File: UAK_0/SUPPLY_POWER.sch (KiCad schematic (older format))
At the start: 23 parts, among them X1 Крепежное_отверстие_d2, X2 Крепежное_отверстие_d2, X3 Крепежное_отверстие_d2

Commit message: BOOT&PRG, концевик, ЖК, звук, подсветка - без трассировки
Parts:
- R1: INFO 100кОм -> 100 кОм
- R2: INFO 6,8кОм -> 6,8 кОм
- R3: INFO 44,2кОм -> 44,2 кОм
- R4: INFO 10кОм -> 10 кОм
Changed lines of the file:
@@
 EESchema Schematic File Version 4
+LIBS:UAK_0-cache
 EELAYER 30 0
 EELAYER END
@@
 F 2 "N_RLC:Конденсатор_SMD_0603" H 5650 2750 60  0001 C CNN
 F 3 "" H 5650 2750 60  0001 C CNN
-F 4 "10нФ/100В" H 5650 2850 50  0000 C CNN "INFO"
+F 4 "10нФ/100В" H 5700 2850 50  0000 C CNN "INFO"
 F 5 "https://www.chipdip.ru/product/grm188r72a103ka01d" H 5650 2750 50  0001 C CNN "LINK"
 	1    5650 2750
@@
 F 2 "N_RLC:Резистор_SMD_0603_0,065_Вт" H 3200 2900 60  0001 C CNN
 F 3 "" H 3200 2900 60  0001 C CNN
-F 4 "100кОм" H 3200 2750 50  0000 C CNN "INFO"
+F 4 "100 кОм" H 3200 2750 50  0000 C CNN "INFO"
 F 5 "" H 3200 3048 50  0001 C CNN "LINK"
 	1    3200 2900
@@
 F 2 "N_RLC:Резистор_SMD_0603_0,065_Вт" H 3250 3550 60  0001 C CNN
 F 3 "" H 3250 3550 60  0001 C CNN
-F 4 "6,8кОм" V 3303 3653 50  0000 L CNN "INFO"
+F 4 "6,8 кОм" V 3303 3653 50  0000 L CNN "INFO"
 F 5 "" H 3250 3698 50  0001 C CNN "LINK"
 	1    3250 3550
@@
 F 2 "N_RLC:Резистор_SMD_0603_0,065_Вт" H 7000 4550 60  0001 C CNN
 F 3 "" H 7000 4550 60  0001 C CNN
-F 4 "10кОм" V 7050 4200 50  0000 L CNN "INFO"
+F 4 "10 кОм" V 7050 4150 50  0000 L CNN "INFO"
 F 5 "" H 7000 4698 50  0001 C CNN "LINK"
 	1    7000 4550
@@
 F 2 "N_RLC:Резистор_SMD_0603_0,065_Вт" H 7000 3550 60  0001 C CNN
 F 3 "" H 7000 3550 60  0001 C CNN
-F 4 "44,2кОм" V 7050 3150 50  0000 L CNN "INFO"
+F 4 "44,2 кОм" V 7050 3100 50  0000 L CNN "INFO"
 F 5 "" H 7000 3698 50  0001 C CNN "LINK"
 	1    7000 3550
@@
 	7000 3850 7000 4050
 Wire Wire Line
-	5000 3200 5500 3200
-Text Label 5500 3200 2    50   ~ 0
+	5000 3200 5250 3200
+Text Label 5250 3200 2    50   ~ 0
 GND
 Wire Wire Line
@@
 Wire Wire Line
 	3500 2900 3850 2900
-Text Label 5500 2900 2    50   ~ 0
+Text Label 5250 2900 2    50   ~ 0
 12V
 Wire Wire Line
-	5500 2900 5000 2900
+	5250 2900 5000 2900
 Text Label 2250 2900 0    50   ~ 0
 12V

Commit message: нет коммутации 220В, остальная схема есть, нет трассировка
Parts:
- added VD4, VD5: Диод_шоттки_SK16, N_VD_HL:Диод_SMB, symbol elements_2020:Диод_шоттки_SK16
- renumbered C4 to C10, C5 to C11, C7 to C12, C6 to C13, C9 to C14, C10 to C15, C8 to C16, C1 to C7, C2 to C8, C3 to C9, DD1 to DD2, R1 to R15, R2 to R16, R3 to R17, R4 to R18, X1 to X5, X2 to X6, X3 to X7
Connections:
- net at C13.1, L2.6: now also VD4.2, VD5.2; no longer G1.+V
- net 0V_RESERV: now reaches C13.2, G1.-V, L2.4
- new net: G1.+V, VD5.1
- new net 12V_RESERV: VD4.1
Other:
- moved on the sheet: C11, C12, C13, C14, C15, C16, C7, C8, C9, DD2, G2, L1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

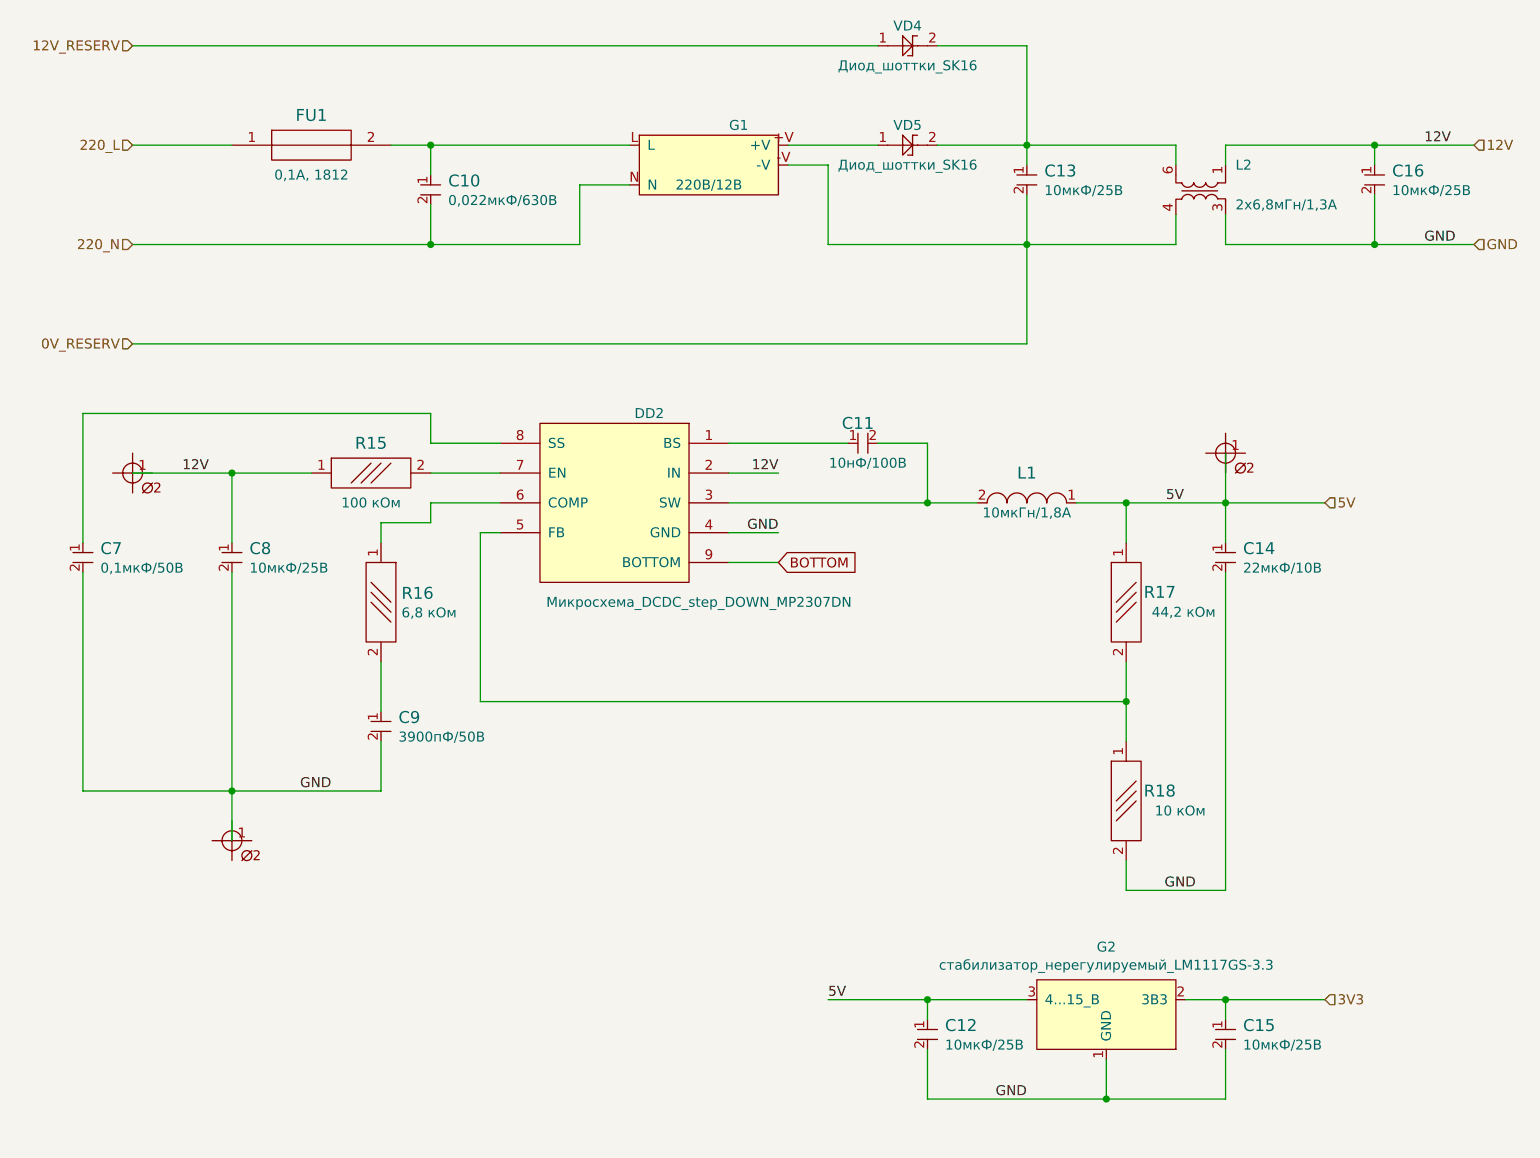
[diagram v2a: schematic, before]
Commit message: подготовлена схема, нет трассировки
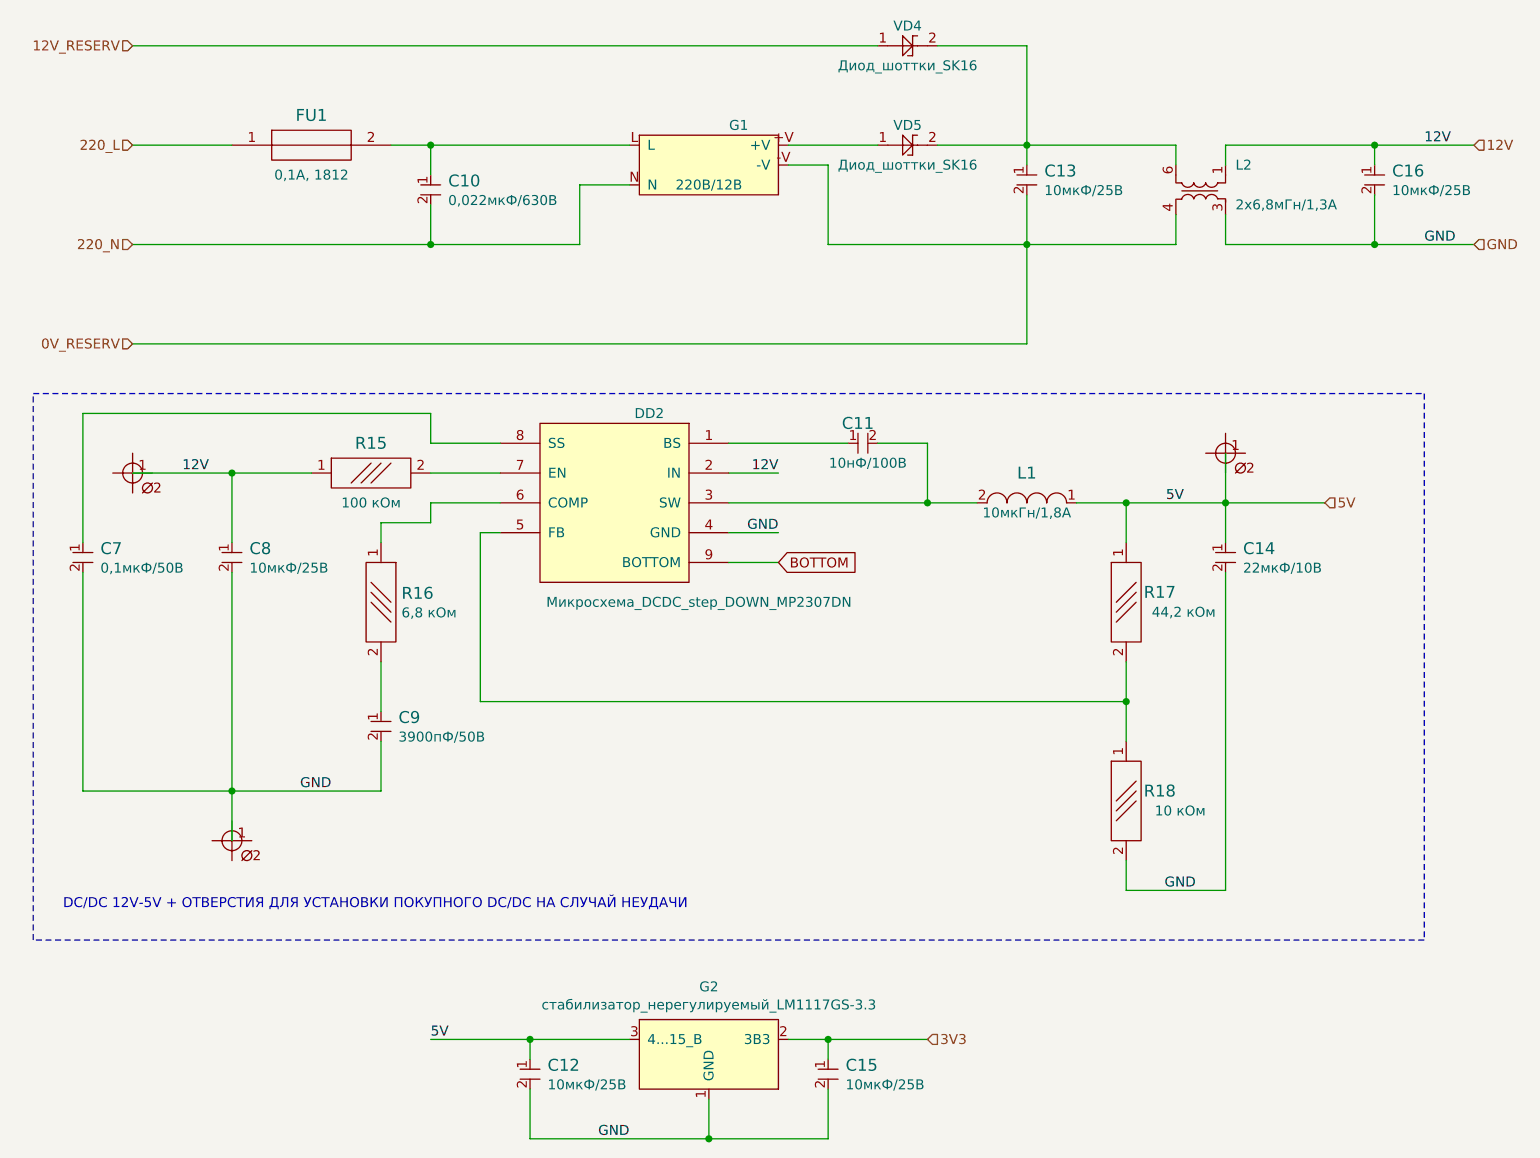
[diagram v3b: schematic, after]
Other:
- note added: "DC/DC 12V-5V + ОТВЕРСТИЯ ДЛЯ УСТАНОВКИ ПОКУПНОГО DC/DC НА СЛУЧАЙ НЕУДАЧИ"
- moved on the sheet: C12, C15, G2
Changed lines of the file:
@@
 Text HLabel 8750 2000 2    50   Input ~ 0
 GND
-Text HLabel 8000 5800 2    50   Input ~ 0
+Text HLabel 6000 6000 2    50   Input ~ 0
 3V3
 Text HLabel 8000 3300 2    50   Input ~ 0
@@
 L elements:стабилизатор_нерегулируемый_LM1117S33 G2
 U 1 1 5F5A8D81
-P 6550 5800
-F 0 "G2" H 6900 6065 50  0000 C CNN
-F 1 "стабилизатор_нерегулируемый_LM1117GS-3.3" H 6900 5974 50  0000 C CNN
-F 2 "N_VD_HL:Транзистор_NPN_SOT223" H 6550 5800 50  0001 C CNN
-F 3 "https://static.chipdip.ru/lib/138/DOC004138838.pdf" H 6550 5800 50  0001 C CNN
-F 4 "https://www.chipdip.ru/product/lm1117gs-3.3" H 6550 5800 50  0001 C CNN "LINK"
-	1    6550 5800
+P 4550 6000
+F 0 "G2" H 4900 6265 50  0000 C CNN
+F 1 "стабилизатор_нерегулируемый_LM1117GS-3.3" H 4900 6174 50  0000 C CNN
+F 2 "N_VD_HL:Транзистор_NPN_SOT223" H 4550 6000 50  0001 C CNN
+F 3 "https://static.chipdip.ru/lib/138/DOC004138838.pdf" H 4550 6000 50  0001 C CNN
+F 4 "https://www.chipdip.ru/product/lm1117gs-3.3" H 4550 6000 50  0001 C CNN "LINK"
+	1    4550 6000
 	1    0    0    -1
 $EndComp
@@
 L elements:Конденсатор_керамический C?
 U 1 1 5F5A914F
-P 6000 5950
+P 4000 6150
 AR Path="/5F5A914F" Ref="C?"  Part="1"
 AR Path="/5F540B17/5F5A914F" Ref="C12"  Part="1"
-F 0 "C12" V 5980 6038 60  0000 L CNN
-F 1 "Конденсатор_керамический" H 6100 5850 60  0001 C CNN
-F 2 "N_RLC:Конденсатор_SMD_0603" H 6000 5950 60  0001 C CNN
-F 3 "" H 6000 5950 60  0001 C CNN
-F 4 "10мкФ/25В" V 6078 6038 50  0000 L CNN "INFO"
-F 5 "https://www.chipdip.ru/product/grm188r61e106m" H 6000 5950 50  0001 C CNN "LINK"
-	1    6000 5950
+F 0 "C12" V 3980 6238 60  0000 L CNN
+F 1 "Конденсатор_керамический" H 4100 6050 60  0001 C CNN
+F 2 "N_RLC:Конденсатор_SMD_0603" H 4000 6150 60  0001 C CNN
+F 3 "" H 4000 6150 60  0001 C CNN
+F 4 "10мкФ/25В" V 4078 6238 50  0000 L CNN "INFO"
+F 5 "https://www.chipdip.ru/product/grm188r61e106m" H 4000 6150 50  0001 C CNN "LINK"
+	1    4000 6150
 	0    1    1    0
 $EndComp
@@
 L elements:Конденсатор_керамический C?
 U 1 1 5F5AA72C
-P 7500 5950
+P 5500 6150
 AR Path="/5F5AA72C" Ref="C?"  Part="1"
 AR Path="/5F540B17/5F5AA72C" Ref="C15"  Part="1"
-F 0 "C15" V 7480 6038 60  0000 L CNN
-F 1 "Конденсатор_керамический" H 7600 5850 60  0001 C CNN
-F 2 "N_RLC:Конденсатор_SMD_0603" H 7500 5950 60  0001 C CNN
-F 3 "" H 7500 5950 60  0001 C CNN
-F 4 "10мкФ/25В" V 7578 6038 50  0000 L CNN "INFO"
-F 5 "https://www.chipdip.ru/product/grm188r61e106m" H 7500 5950 50  0001 C CNN "LINK"
-	1    7500 5950
-	0    1    1    0
-$EndComp
-Wire Wire Line
-	7300 5800 7500 5800
-Wire Wire Line
-	7500 5800 7500 5900
-Wire Wire Line
-	7500 6050 7500 6300
-Wire Wire Line
-	7500 6300 6900 6300
-Wire Wire Line
-	6000 6300 6000 6050
-Wire Wire Line
-	6000 5900 6000 5800
-Wire Wire Line
-	6000 5800 6500 5800
-Connection ~ 6900 6300
-Wire Wire Line
-	6900 6300 6000 6300
-Wire Wire Line
-	6900 6100 6900 6300
-Text Label 6500 6300 2    50   ~ 0
+F 0 "C15" V 5480 6238 60  0000 L CNN
+F 1 "Конденсатор_керамический" H 5600 6050 60  0001 C CNN
+F 2 "N_RLC:Конденсатор_SMD_0603" H 5500 6150 60  0001 C CNN
+F 3 "" H 5500 6150 60  0001 C CNN
+F 4 "10мкФ/25В" V 5578 6238 50  0000 L CNN "INFO"
+F 5 "https://www.chipdip.ru/product/grm188r61e106m" H 5500 6150 50  0001 C CNN "LINK"
+	1    5500 6150
+	0    1    1    0
+$EndComp
+Wire Wire Line
+	5300 6000 5500 6000
+Wire Wire Line
+	5500 6000 5500 6100
+Wire Wire Line
+	5500 6250 5500 6500
+Wire Wire Line
+	5500 6500 4900 6500
+Wire Wire Line
+	4000 6500 4000 6250
+Wire Wire Line
+	4000 6100 4000 6000
+Wire Wire Line
+	4000 6000 4500 6000
+Connection ~ 4900 6500
+Wire Wire Line
+	4900 6500 4000 6500
+Wire Wire Line
+	4900 6300 4900 6500
+Text Label 4500 6500 2    50   ~ 0
 GND
 Wire Wire Line
-	6000 5800 5500 5800
-Connection ~ 6000 5800
-Wire Wire Line
-	7500 5800 8000 5800
-Connection ~ 7500 5800
+	4000 6000 3500 6000
+Connection ~ 4000 6000
+Wire Wire Line
+	5500 6000 6000 6000
+Connection ~ 5500 6000
 Text Label 7200 3300 0    50   ~ 0
 5V
-Text Label 5500 5800 0    50   ~ 0
+Text Label 3500 6000 0    50   ~ 0
 5V
 $Comp
@@
 Wire Wire Line
 	6500 2500 6500 2000
+Wire Notes Line
+	1500 2750 8500 2750
+Wire Notes Line
+	8500 2750 8500 5500
+Wire Notes Line
+	8500 5500 1500 5500
+Wire Notes Line
+	1500 5500 1500 2750
+Text Notes 1650 5350 0    50   ~ 0
+DC/DC 12V-5V + ОТВЕРСТИЯ ДЛЯ УСТАНОВКИ ПОКУПНОГО DC/DC НА СЛУЧАЙ НЕУДАЧИ
 $EndSCHEMATC

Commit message: есть трассировка питания
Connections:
- net 12V_OUT_G: now reaches G1.+V, VD5.1
- net 220_L_FU: now reaches C10.1, FU1.2, G1.L
- net 12V_NOISE: now reaches C13.1, L2.6, VD4.2, VD5.2
- net 5V_DC-DC: now reaches C11.2, DD2.3 (SW), L1.2
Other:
- moved on the sheet: VD4, VD5
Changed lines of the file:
@@
 L elements_2020:Диод_шоттки_SK16 VD?
 U 1 1 5F83EC0D
-P 5750 1000
+P 6000 1000
 AR Path="/5F83EC0D" Ref="VD?"  Part="1"
 AR Path="/5F540B17/5F83EC0D" Ref="VD4"  Part="1"
-F 0 "VD4" H 5900 1100 50  0000 C CNN
-F 1 "Диод_шоттки_SK16" H 5900 900 50  0000 C CNN
-F 2 "N_VD_HL:Диод_SMB" H 5925 775 50  0001 C CNN
-F 3 "https://static.chipdip.ru/lib/046/DOC003046730.pdf" H 5650 1000 50  0001 C CNN
-F 4 "1А, 60В" H 5925 550 50  0001 C CNN "INFO"
-F 5 "https://www.chipdip.ru/product/sk16-diotec" H 5925 675 50  0001 C CNN "LINK"
-	1    5750 1000
+F 0 "VD4" H 6150 1100 50  0000 C CNN
+F 1 "Диод_шоттки_SK16" H 6050 900 50  0000 C CNN
+F 2 "N_VD_HL:Диод_SMB" H 6175 775 50  0001 C CNN
+F 3 "https://static.chipdip.ru/lib/046/DOC003046730.pdf" H 5900 1000 50  0001 C CNN
+F 4 "1А, 60В" H 6175 550 50  0001 C CNN "INFO"
+F 5 "https://www.chipdip.ru/product/sk16-diotec" H 6175 675 50  0001 C CNN "LINK"
+	1    6000 1000
 	1    0    0    -1
 $EndComp
@@
 L elements_2020:Диод_шоттки_SK16 VD?
 U 1 1 5F8429E0
-P 5750 1500
+P 6000 1500
 AR Path="/5F8429E0" Ref="VD?"  Part="1"
 AR Path="/5F540B17/5F8429E0" Ref="VD5"  Part="1"
-F 0 "VD5" H 5900 1600 50  0000 C CNN
-F 1 "Диод_шоттки_SK16" H 5900 1400 50  0000 C CNN
-F 2 "N_VD_HL:Диод_SMB" H 5925 1275 50  0001 C CNN
-F 3 "https://static.chipdip.ru/lib/046/DOC003046730.pdf" H 5650 1500 50  0001 C CNN
-F 4 "1А, 60В" H 5925 1050 50  0001 C CNN "INFO"
-F 5 "https://www.chipdip.ru/product/sk16-diotec" H 5925 1175 50  0001 C CNN "LINK"
-	1    5750 1500
+F 0 "VD5" H 6150 1600 50  0000 C CNN
+F 1 "Диод_шоттки_SK16" H 6050 1400 50  0000 C CNN
+F 2 "N_VD_HL:Диод_SMB" H 6175 1275 50  0001 C CNN
+F 3 "https://static.chipdip.ru/lib/046/DOC003046730.pdf" H 5900 1500 50  0001 C CNN
+F 4 "1А, 60В" H 6175 1050 50  0001 C CNN "INFO"
+F 5 "https://www.chipdip.ru/product/sk16-diotec" H 6175 1175 50  0001 C CNN "LINK"
+	1    6000 1500
 	1    0    0    -1
 $EndComp
 Wire Wire Line
-	6050 1500 6500 1500
+	6300 1500 6500 1500
 Wire Wire Line
-	5750 1500 5300 1500
+	6000 1500 5300 1500
 Wire Wire Line
 	5500 2000 6500 2000
 Connection ~ 6500 2000
 Wire Wire Line
-	6050 1000 6500 1000
+	6300 1000 6500 1000
 Wire Wire Line
-	5750 1000 2000 1000
+	6000 1000 2000 1000
 Text HLabel 2000 2500 0    50   Input ~ 0
 0V_RESERV
@@
 Text Notes 1650 5350 0    50   ~ 0
 DC/DC 12V-5V + ОТВЕРСТИЯ ДЛЯ УСТАНОВКИ ПОКУПНОГО DC/DC НА СЛУЧАЙ НЕУДАЧИ
+Text Label 4000 1500 2    50   ~ 0
+220_L_FU
+Text Label 7000 1500 2    50   ~ 0
+12V_NOISE
+Text Label 5500 1500 0    50   ~ 0
+12V_OUT_G
+Text Label 5500 3300 0    50   ~ 0
+5V_DC-DC
 $EndSCHEMATC

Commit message: начата установка ESP32
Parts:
- DD2: symbol elements_2020:Микросхема_DCDC_step_DOWN_MP2307DN -> UAK_0-rescue:Микросхема_DCDC_step_DOWN_MP2307DN-elements_2020
- G1: symbol elements_2020:AC-DC-преобразователь_IRM-20-12 -> UAK_0-rescue:AC-DC-преобразователь_IRM-20-12-elements_2020
- L1: symbol elements_2020:Чип-индуктивность_10мкГн_1.8А_20проц. -> UAK_0-rescue:Чип-индуктивность_10мкГн_1.8А_20проц.-elements_2020
- L2: symbol elements_2020:Дроссель_B82731-T2132-A20_2х6.8мГн_1.3А_250В -> UAK_0-rescue:Дроссель_B82731-T2132-A20_2х6.8мГн_1.3А_250В-elements_2020
- VD4, VD5: symbol elements_2020:Диод_шоттки_SK16 -> UAK_0-rescue:Диод_шоттки_SK16-elements_2020
- X5, X6, X7: symbol MOTOR_2020_components:Крепежное_отверстие_d2 -> UAK_0-rescue:Крепежное_отверстие_d2-MOTOR_2020_components
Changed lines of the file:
@@
 EESchema Schematic File Version 4
 LIBS:UAK_0-cache
-EELAYER 30 0
+EELAYER 29 0
 EELAYER END
 $Descr A4 11693 8268
@@
 $EndDescr
 $Comp
-L elements_2020:AC-DC-преобразователь_IRM-20-12 G?
+L UAK_0-rescue:AC-DC-преобразователь_IRM-20-12-elements_2020 G?
 U 1 1 5F542179
 P 4550 1500
@@
 	6500 1600 6500 1500
 $Comp
-L elements_2020:Дроссель_B82731-T2132-A20_2х6.8мГн_1.3А_250В L2
+L UAK_0-rescue:Дроссель_B82731-T2132-A20_2х6.8мГн_1.3А_250В-elements_2020 L2
 U 1 1 5F5455B1
 P 7500 1600
@@
 Connection ~ 8250 2000
 $Comp
-L elements_2020:Микросхема_DCDC_step_DOWN_MP2307DN DD2
+L UAK_0-rescue:Микросхема_DCDC_step_DOWN_MP2307DN-elements_2020 DD2
 U 1 1 5F552963
 P 4800 3000
@@
 $EndComp
 $Comp
-L elements_2020:Чип-индуктивность_10мкГн_1.8А_20проц. L1
+L UAK_0-rescue:Чип-индуктивность_10мкГн_1.8А_20проц.-elements_2020 L1
 U 1 1 5F554A99
 P 6300 3300
@@
 5V
 $Comp
-L MOTOR_2020_components:Крепежное_отверстие_d2 X5
+L UAK_0-rescue:Крепежное_отверстие_d2-MOTOR_2020_components X5
 U 1 1 5F5BE478
 P 2000 3150
@@
 	2000 3150 2500 3150
 $Comp
-L MOTOR_2020_components:Крепежное_отверстие_d2 X6
+L UAK_0-rescue:Крепежное_отверстие_d2-MOTOR_2020_components X6
 U 1 1 5F5C4713
 P 2500 5000
@@
 	2500 4750 2500 5000
 $Comp
-L MOTOR_2020_components:Крепежное_отверстие_d2 X7
+L UAK_0-rescue:Крепежное_отверстие_d2-MOTOR_2020_components X7
 U 1 1 5F5CB41B
 P 7500 3050
@@
 	6500 1000 6500 1500
 $Comp
-L elements_2020:Диод_шоттки_SK16 VD?
+L UAK_0-rescue:Диод_шоттки_SK16-elements_2020 VD?
 U 1 1 5F83EC0D
 P 6000 1000
@@
 $EndComp
 $Comp
-L elements_2020:Диод_шоттки_SK16 VD?
+L UAK_0-rescue:Диод_шоттки_SK16-elements_2020 VD?
 U 1 1 5F8429E0
 P 6000 1500
